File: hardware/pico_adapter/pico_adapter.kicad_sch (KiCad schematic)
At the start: 39 parts, among them J1 L77HDE15SD1CH4F, J2 AudioJack2_Ground, Q1 Q_NMOS_DGS, Q2 Q_NMOS_DGS

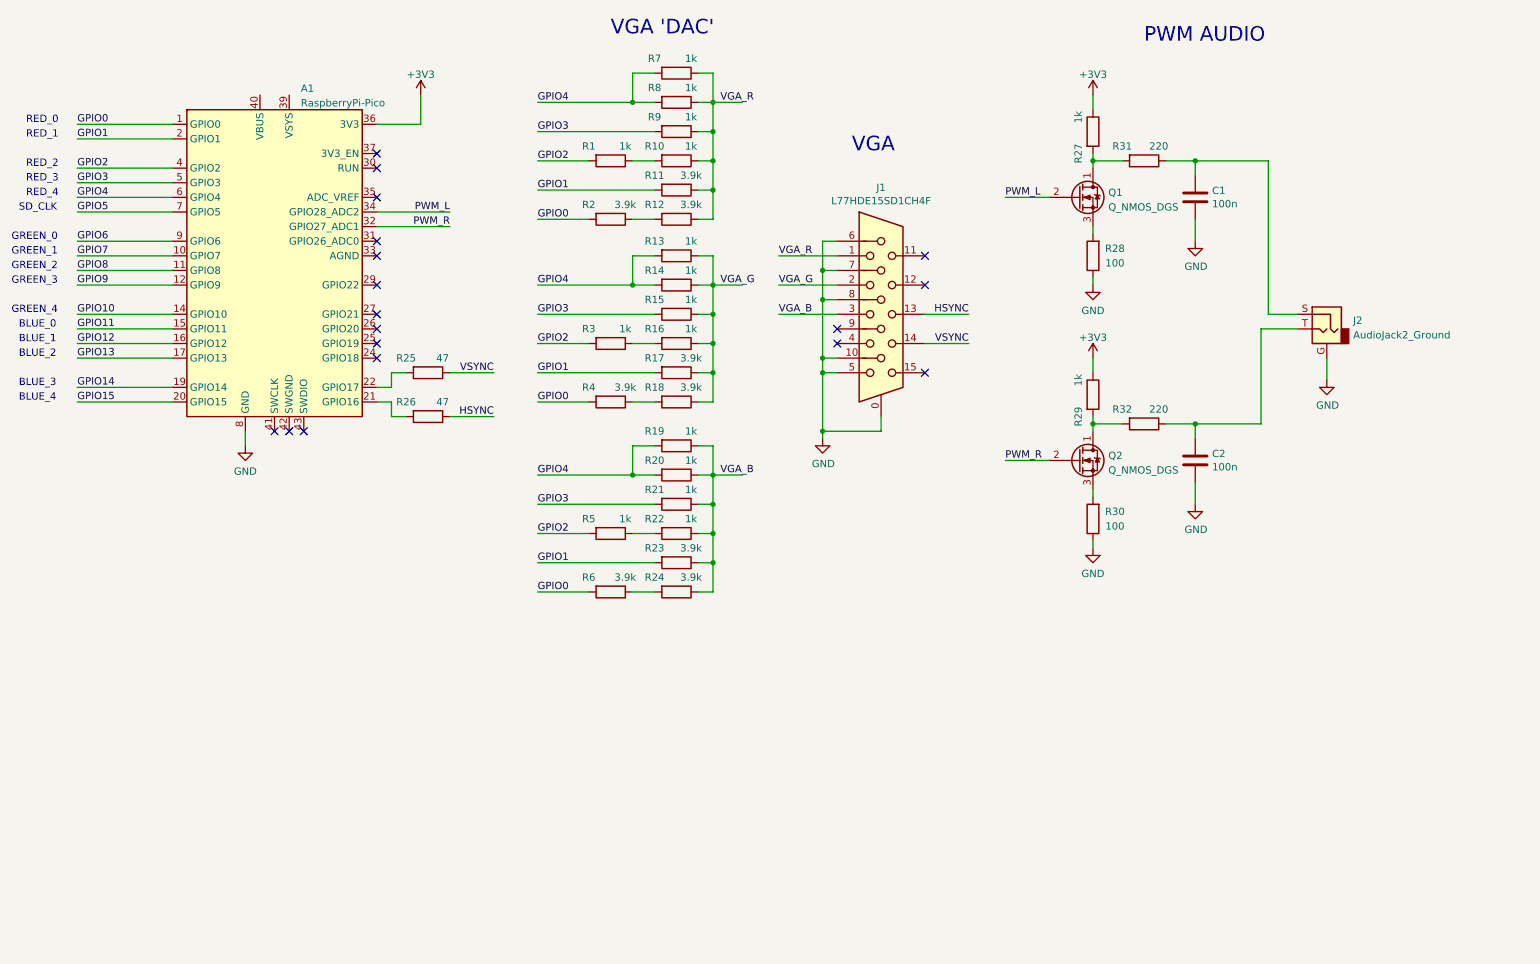
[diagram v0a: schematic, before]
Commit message: added gitignore + Power section
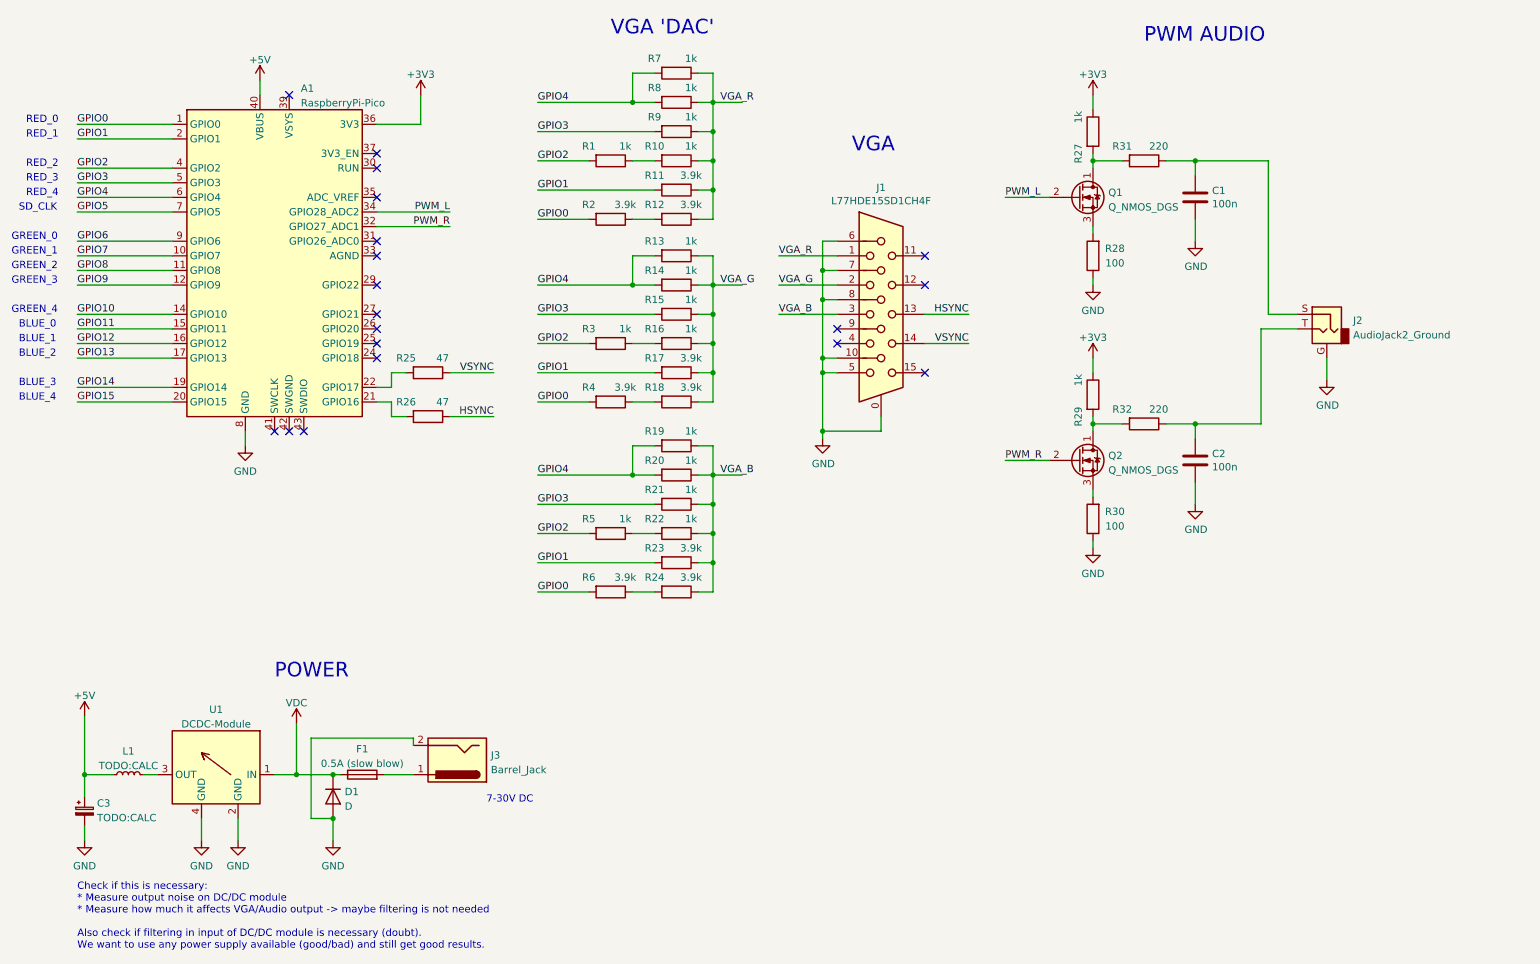
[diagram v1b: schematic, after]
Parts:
- added C3: TODO:CALC, symbol Device:C_Polarized_Small
- added D1: D, Diode_THT:D_A-405_P10.16mm_Horizontal, symbol Device:D
- added F1: 0.5A (slow blow), Fuse:Fuseholder_Cylinder-5x20mm_Schurter_0031_8201_Horizontal_Open, symbol Device:Fuse
- added J3: Barrel_Jack, Connector_BarrelJack:BarrelJack_CUI_PJ-102AH_Horizontal, symbol Connector:Barrel_Jack
- added L1: TODO:CALC, symbol Device:L_Small
- added U1: DCDC-Module, symbol pico_adapter_specific:DCDC-Module
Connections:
- net GND: now also C3.2, D1.2 (A), J3.2, U1.2 (GND), U1.4 (GND)
- net +5V: now reaches A1.40 (VBUS)
- net +5V: now also C3.1, L1.1
- new net: F1.2, J3.1
- new net: L1.2, U1.3 (OUT)
- new net VDC: D1.1 (K), F1.1, U1.1 (IN)
- no-connect marks 18 -> 19
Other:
- note added: "7-30V DC"
- note added: "Check if this is necessary: * Measure output noise on DC/DC module * Measure how much it affects VGA/Audio output -> maybe filtering is not needed Also check if filtering in input of DC/DC module is necessary (doubt). We want to use any power supply available (good/bad) and still get good results."
- note added: "POWER"

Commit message: added DC decoupling on output
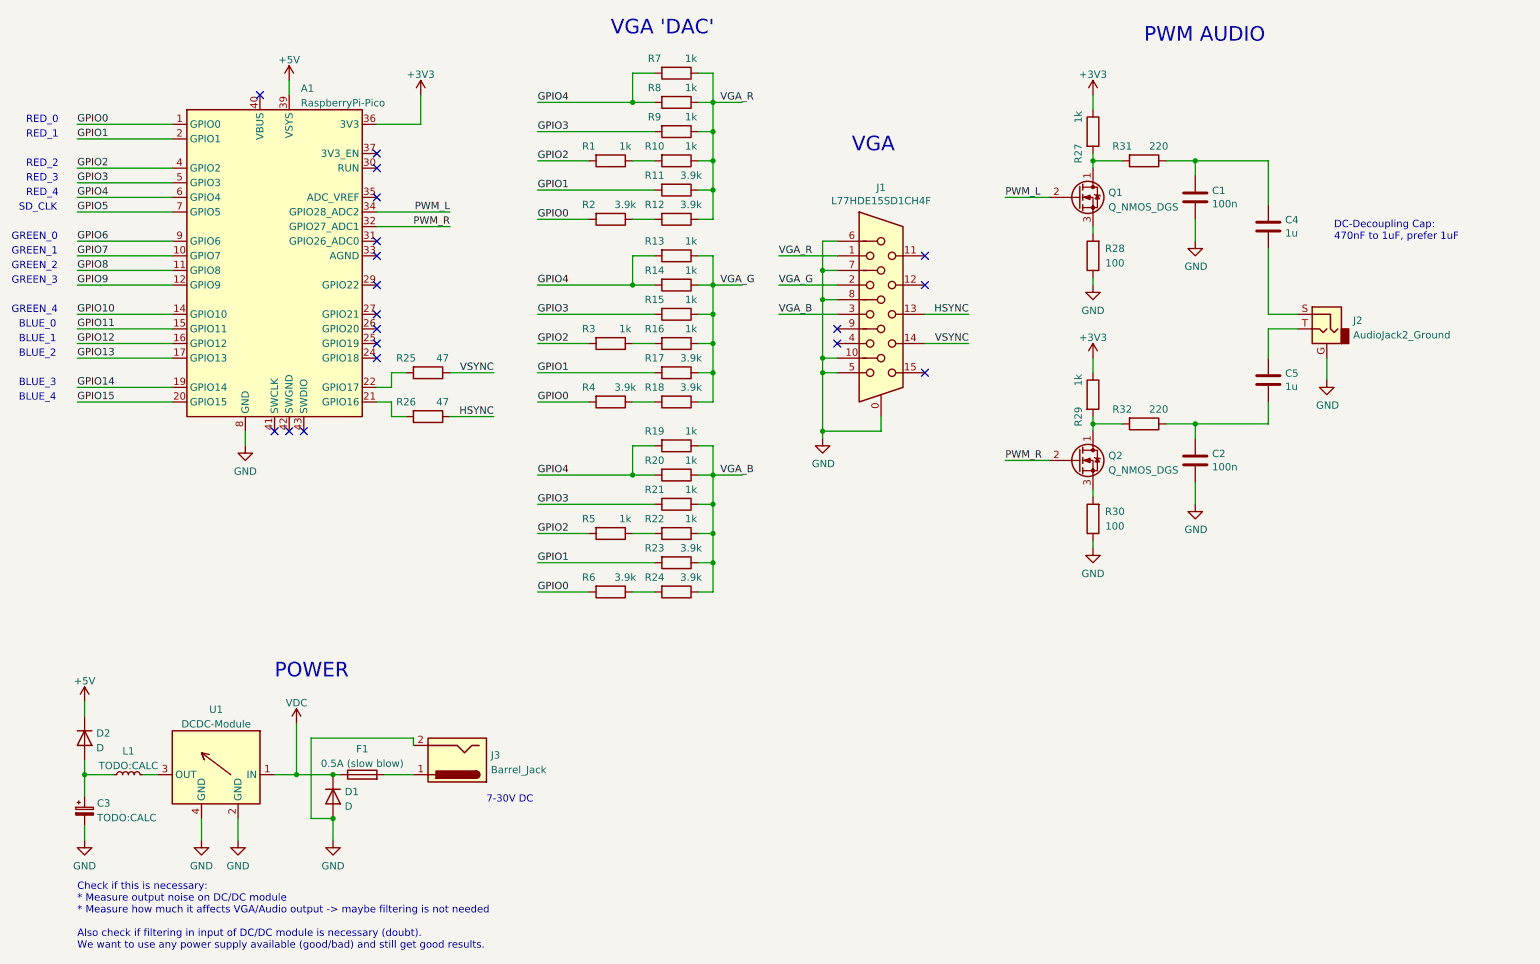
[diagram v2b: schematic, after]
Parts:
- added C4, C5: 1u, Capacitor_SMD:C_0402_1005Metric, symbol Device:C
- added D2: D, symbol Device:D
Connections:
- net +5V: now also A1.39 (VSYS), D2.1 (K); no longer A1.40 (VBUS), C3.1, L1.1
- net at C1.1, R31.1: now also C4.1; no longer J2.S
- net at C2.1, R32.1: now also C5.2; no longer J2.T
- new net: C3.1, D2.2 (A), L1.1
- new net: C5.1, J2.T
- new net: C4.2, J2.S
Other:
- note added: "DC-Decoupling Cap: 470nF to 1uF, prefer 1uF"
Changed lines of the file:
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@@
   (junction (at 137.16 110.49) (diameter 0) (color 0 0 0 0)
   )
+  (junction (at 137.16 100.33) (diameter 0) (color 0 0 0 0)
+  )
+  (junction (at 123.19 95.25) (diameter 0) (color 0 0 0 0)
+  )
+  (junction (at 203.2 40.64) (diameter 0) (color 0 0 0 0)
+  )
+  (junction (at 156.21 77.47) (diameter 0) (color 0 0 0 0)
+  )
+  (junction (at 156.21 87.63) (diameter 0) (color 0 0 0 0)
+  )
+  (junction (at 123.19 30.48) (diameter 0) (color 0 0 0 0)
+  )
+  (junction (at 137.16 95.25) (diameter 0) (color 0 0 0 0)
+  )
+  (junction (at 64.77 147.32) (diameter 0) (color 0 0 0 0)
+  )
+  (junction (at 137.16 35.56) (diameter 0) (color 0 0 0 0)
+  )
   (junction (at 27.94 147.32) (diameter 0) (color 0 0 0 0)
-  )
-  (junction (at 137.16 100.33) (diameter 0) (color 0 0 0 0)
-  )
-  (junction (at 123.19 95.25) (diameter 0) (color 0 0 0 0)
-  )
-  (junction (at 203.2 40.64) (diameter 0) (color 0 0 0 0)
-  )
-  (junction (at 156.21 77.47) (diameter 0) (color 0 0 0 0)
-  )
-  (junction (at 156.21 87.63) (diameter 0) (color 0 0 0 0)
-  )
-  (junction (at 123.19 30.48) (diameter 0) (color 0 0 0 0)
-  )
-  (junction (at 137.16 95.25) (diameter 0) (color 0 0 0 0)
-  )
-  (junction (at 64.77 147.32) (diameter 0) (color 0 0 0 0)
-  )
-  (junction (at 137.16 35.56) (diameter 0) (color 0 0 0 0)
   )
   (junction (at 137.16 30.48) (diameter 0) (color 0 0 0 0)
@@
   (no_connect (at 78.74 67.31))
   (no_connect (at 78.74 72.39))
-  (no_connect (at 63.5 29.21))
+  (no_connect (at 58.42 29.21))
   (no_connect (at 78.74 41.91))
   (no_connect (at 173.99 62.23))
@@
     (stroke (width 0) (type default) (color 0 0 0 0))
   )
+  (wire (pts (xy 233.68 69.85) (xy 238.76 69.85))
+    (stroke (width 0) (type default) (color 0 0 0 0))
+  )
   (wire (pts (xy 64.77 147.32) (xy 71.12 147.32))
     (stroke (width 0) (type default) (color 0 0 0 0))
@@
     (stroke (width 0) (type default) (color 0 0 0 0))
   )
-  (wire (pts (xy 58.42 26.67) (xy 58.42 29.21))
+  (wire (pts (xy 63.5 26.67) (xy 63.5 29.21))
     (stroke (width 0) (type default) (color 0 0 0 0))
   )
@@
     (stroke (width 0) (type default) (color 0 0 0 0))
   )
+  (wire (pts (xy 233.68 82.55) (xy 233.68 86.36))
+    (stroke (width 0) (type default) (color 0 0 0 0))
+  )
   (wire (pts (xy 158.75 54.61) (xy 156.21 54.61))
     (stroke (width 0) (type default) (color 0 0 0 0))
@@
     (stroke (width 0) (type default) (color 0 0 0 0))
   )
+  (wire (pts (xy 27.94 144.78) (xy 27.94 147.32))
+    (stroke (width 0) (type default) (color 0 0 0 0))
+  )
   (wire (pts (xy 64.77 138.43) (xy 64.77 147.32))
     (stroke (width 0) (type default) (color 0 0 0 0))
@@
     (stroke (width 0) (type default) (color 0 0 0 0))
   )
+  (wire (pts (xy 27.94 134.62) (xy 27.94 137.16))
+    (stroke (width 0) (type default) (color 0 0 0 0))
+  )
   (wire (pts (xy 203.2 106.68) (xy 203.2 107.95))
     (stroke (width 0) (type default) (color 0 0 0 0))
@@
     (stroke (width 0) (type default) (color 0 0 0 0))
   )
-  (wire (pts (xy 232.41 86.36) (xy 232.41 69.85))
-    (stroke (width 0) (type default) (color 0 0 0 0))
-  )
   (wire (pts (xy 81.28 82.55) (xy 81.28 85.09))
     (stroke (width 0) (type default) (color 0 0 0 0))
@@
     (stroke (width 0) (type default) (color 0 0 0 0))
   )
-  (wire (pts (xy 27.94 137.16) (xy 27.94 147.32))
-    (stroke (width 0) (type default) (color 0 0 0 0))
-  )
   (wire (pts (xy 26.67 67.31) (xy 43.18 67.31))
     (stroke (width 0) (type default) (color 0 0 0 0))
@@
     (stroke (width 0) (type default) (color 0 0 0 0))
   )
-  (wire (pts (xy 232.41 69.85) (xy 238.76 69.85))
-    (stroke (width 0) (type default) (color 0 0 0 0))
-  )
-  (wire (pts (xy 233.68 40.64) (xy 233.68 67.31))
-    (stroke (width 0) (type default) (color 0 0 0 0))
-  )
   (wire (pts (xy 86.36 34.29) (xy 86.36 29.21))
     (stroke (width 0) (type default) (color 0 0 0 0))
@@
     (stroke (width 0) (type default) (color 0 0 0 0))
   )
+  (wire (pts (xy 233.68 40.64) (xy 233.68 48.26))
+    (stroke (width 0) (type default) (color 0 0 0 0))
+  )
   (wire (pts (xy 134.62 25.4) (xy 137.16 25.4))
     (stroke (width 0) (type default) (color 0 0 0 0))
@@
     (stroke (width 0) (type default) (color 0 0 0 0))
   )
-  (wire (pts (xy 220.98 86.36) (xy 232.41 86.36))
+  (wire (pts (xy 220.98 86.36) (xy 233.68 86.36))
     (stroke (width 0) (type default) (color 0 0 0 0))
   )
@@
     (stroke (width 0) (type default) (color 0 0 0 0))
   )
+  (wire (pts (xy 233.68 69.85) (xy 233.68 74.93))
+    (stroke (width 0) (type default) (color 0 0 0 0))
+  )
   (wire (pts (xy 137.16 25.4) (xy 137.16 30.48))
     (stroke (width 0) (type default) (color 0 0 0 0))
   )
+  (wire (pts (xy 233.68 55.88) (xy 233.68 67.31))
+    (stroke (width 0) (type default) (color 0 0 0 0))
+  )
   (wire (pts (xy 134.62 45.72) (xy 137.16 45.72))
     (stroke (width 0) (type default) (color 0 0 0 0))
+  )
+  (text "DC-Decoupling Cap:\n470nF to 1uF, prefer 1uF" (at 245.11 54.61 0)
+    (effects (font (size 1.27 1.27)) (justify left bottom))
   )
   (text "POWER" (at 60.96 130.81 0)
@@
     (pin "2")
   )
-  (symbol (lib_id "power:+5V") (at 27.94 137.16 0) (unit 1)
-    (in_bom yes) (on_board yes) (fields_autoplaced)
-    (property "Reference" "#PWR011" (id 0) (at 27.94 140.97 0)
-      (effects (font (size 1.27 1.27)) hide)
-    )
-    (property "Value" "+5V" (id 1) (at 27.94 133.5842 0))
-    (property "Footprint" "" (id 2) (at 27.94 137.16 0)
-      (effects (font (size 1.27 1.27)) hide)
-    )
-    (property "Datasheet" "" (id 3) (at 27.94 137.16 0)
+  (symbol (lib_id "power:+5V") (at 27.94 134.62 0) (unit 1)
+    (in_bom yes) (on_board yes) (fields_autoplaced)
+    (property "Reference" "#PWR011" (id 0) (at 27.94 138.43 0)
+      (effects (font (size 1.27 1.27)) hide)
+    )
+    (property "Value" "+5V" (id 1) (at 27.94 131.0442 0))
+    (property "Footprint" "" (id 2) (at 27.94 134.62 0)
+      (effects (font (size 1.27 1.27)) hide)
+    )
+    (property "Datasheet" "" (id 3) (at 27.94 134.62 0)
       (effects (font (size 1.27 1.27)) hide)
     )
@@
     (pin "2")
   )
+  (symbol (lib_id "Device:D") (at 27.94 140.97 270) (unit 1)
+    (in_bom yes) (on_board yes) (fields_autoplaced)
+    (property "Reference" "D2" (id 0) (at 29.972 140.1353 90)
+      (effects (font (size 1.27 1.27)) (justify left))
+    )
+    (property "Value" "D" (id 1) (at 29.972 142.6722 90)
+      (effects (font (size 1.27 1.27)) (justify left))
+    )
+    (property "Footprint" "" (id 2) (at 27.94 140.97 0)
+      (effects (font (size 1.27 1.27)) hide)
+    )
+    (property "Datasheet" "~" (id 3) (at 27.94 140.97 0)
+      (effects (font (size 1.27 1.27)) hide)
+    )
+    (pin "1")
+    (pin "2")
+  )
   (symbol (lib_id "Device:R") (at 130.81 72.39 270) (unit 1)
     (in_bom yes) (on_board yes)
@@
     (pin "2")
   )
-  (symbol (lib_id "power:+5V") (at 58.42 26.67 0) (unit 1)
-    (in_bom yes) (on_board yes) (fields_autoplaced)
-    (property "Reference" "#PWR0101" (id 0) (at 58.42 30.48 0)
-      (effects (font (size 1.27 1.27)) hide)
-    )
-    (property "Value" "+5V" (id 1) (at 58.42 23.0942 0))
-    (property "Footprint" "" (id 2) (at 58.42 26.67 0)
-      (effects (font (size 1.27 1.27)) hide)
-    )
-    (property "Datasheet" "" (id 3) (at 58.42 26.67 0)
+  (symbol (lib_id "power:+5V") (at 63.5 26.67 0) (unit 1)
+    (in_bom yes) (on_board yes) (fields_autoplaced)
+    (property "Reference" "#PWR0101" (id 0) (at 63.5 30.48 0)
+      (effects (font (size 1.27 1.27)) hide)
+    )
+    (property "Value" "+5V" (id 1) (at 63.5 23.0942 0))
+    (property "Footprint" "" (id 2) (at 63.5 26.67 0)
+      (effects (font (size 1.27 1.27)) hide)
+    )
+    (property "Datasheet" "" (id 3) (at 63.5 26.67 0)
       (effects (font (size 1.27 1.27)) hide)
     )
@@
     (pin "2")
   )
+  (symbol (lib_id "Device:C") (at 233.68 78.74 0) (unit 1)
+    (in_bom yes) (on_board yes)
+    (property "Reference" "C5" (id 0) (at 236.601 77.5716 0)
+      (effects (font (size 1.27 1.27)) (justify left))
+    )
+    (property "Value" "1u" (id 1) (at 236.601 79.883 0)
+      (effects (font (size 1.27 1.27)) (justify left))
+    )
+    (property "Footprint" "Capacitor_SMD:C_0402_1005Metric" (id 2) (at 234.6452 82.55 0)
+      (effects (font (size 1.27 1.27)) hide)
+    )
+    (property "Datasheet" "~" (id 3) (at 233.68 78.74 0)
+      (effects (font (size 1.27 1.27)) hide)
+    )
+    (pin "1")
+    (pin "2")
+  )
   (symbol (lib_id "power:GND") (at 243.84 78.74 0) (unit 1)
     (in_bom yes) (on_board yes)
@@
     )
     (property "Datasheet" "~" (id 3) (at 130.81 57.15 0)
+      (effects (font (size 1.27 1.27)) hide)
+    )
+    (pin "1")
+    (pin "2")
+  )
+  (symbol (lib_id "Device:C") (at 233.68 52.07 0) (unit 1)
+    (in_bom yes) (on_board yes)
+    (property "Reference" "C4" (id 0) (at 236.601 50.9016 0)
+      (effects (font (size 1.27 1.27)) (justify left))
+    )
+    (property "Value" "1u" (id 1) (at 236.601 53.213 0)
+      (effects (font (size 1.27 1.27)) (justify left))
+    )
+    (property "Footprint" "Capacitor_SMD:C_0402_1005Metric" (id 2) (at 234.6452 55.88 0)
+      (effects (font (size 1.27 1.27)) hide)
+    )
+    (property "Datasheet" "~" (id 3) (at 233.68 52.07 0)
       (effects (font (size 1.27 1.27)) hide)
     )
@@
       (reference "C3") (unit 1) (value "TODO:CALC") (footprint "")
     )
+    (path "/80d9d717-f275-4ce8-96c8-5105a1bced0d"
+      (reference "C4") (unit 1) (value "1u") (footprint "Capacitor_SMD:C_0402_1005Metric")
+    )
+    (path "/622eb930-e349-47b4-b267-a1aa943a8443"
+      (reference "C5") (unit 1) (value "1u") (footprint "Capacitor_SMD:C_0402_1005Metric")
+    )
     (path "/58444acc-6296-49c8-a672-8347e56a7d62"
       (reference "D1") (unit 1) (value "D") (footprint "Diode_THT:D_A-405_P10.16mm_Horizontal")
     )
+    (path "/30cf15d3-0800-4d2f-9688-a78d2373ba28"
+      (reference "D2") (unit 1) (value "D") (footprint "")
+    )
     (path "/d472857a-955b-44c5-859e-529ca5eec1b2"

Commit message: added footprints + assigned footprints + minor changes
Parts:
- A1: footprint (none) -> Module:Raspberry_Pi_Pico_Socket
- C1, C2, C4, C5: footprint Capacitor_SMD:C_0402_1005Metric -> Capacitor_THT:C_Rect_L7.5mm_W6.5mm_P5.00mm
- C3: footprint (none) -> Capacitor_THT:CP_Radial_D6.3mm_P2.50mm
- D2: footprint (none) -> Diode_THT:D_A-405_P10.16mm_Horizontal
- J1: footprint RPi_Pico:DSUB-15-L77HDE15SD1CH4F -> Connector_Dsub:DSUB-15-HD_Female_Horizontal_P2.29x1.98mm_EdgePinOffset8.35mm_Housed_MountingHolesOffset10.89mm
- J2: footprint (none) -> Connector_Audio:Jack_3.5mm_CUI_SJ1-3523N_Horizontal; symbol Connector:AudioJack2_Ground -> Connector:AudioJack3
- J3: symbol Connector:Barrel_Jack -> Connector:Barrel_Jack_MountingPin
- L1: footprint (none) -> Inductor_THT:L_Radial_D7.5mm_P3.50mm_Fastron_07P
- Q1, Q2: footprint (none) -> Package_TO_SOT_THT:TO-92_Wide
- R1, R10, R11, R12, R13, R14, R15, R16, R17, R18, R19, R2, R20, R21, R22, R23, R24, R25, R26, R27, R28, R29, R3, R30, R31, R32, R4, R5, R6, R7, R8, R9: footprint Resistor_SMD:R_0402_1005Metric -> Resistor_THT:R_Axial_DIN0204_L3.6mm_D1.6mm_P7.62mm_Horizontal
- U1: footprint (none) -> Module:DCDC-Module
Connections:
- net GND: now also J2.S, J3.MP (MountPin); no longer J2.G
- net at C5.1: now also J2.R; no longer J2.T
- net at C4.2: now also J2.T; no longer J2.S
